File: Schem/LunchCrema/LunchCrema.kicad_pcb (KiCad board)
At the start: 4 copper layers, 160 x 64.4 mm, 52 parts, among them IC1 MMPQ3904, J1 pBITzBus, J3 DE15_Socket_HighDensity_Mount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, SW1 SW_Coded_SH-7070, U1 74HC688, U10 74HC139, U2 V9958, U3 74HC273, U8 74LVC1G19, Y1 HC-49/U-S21477270ABJB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

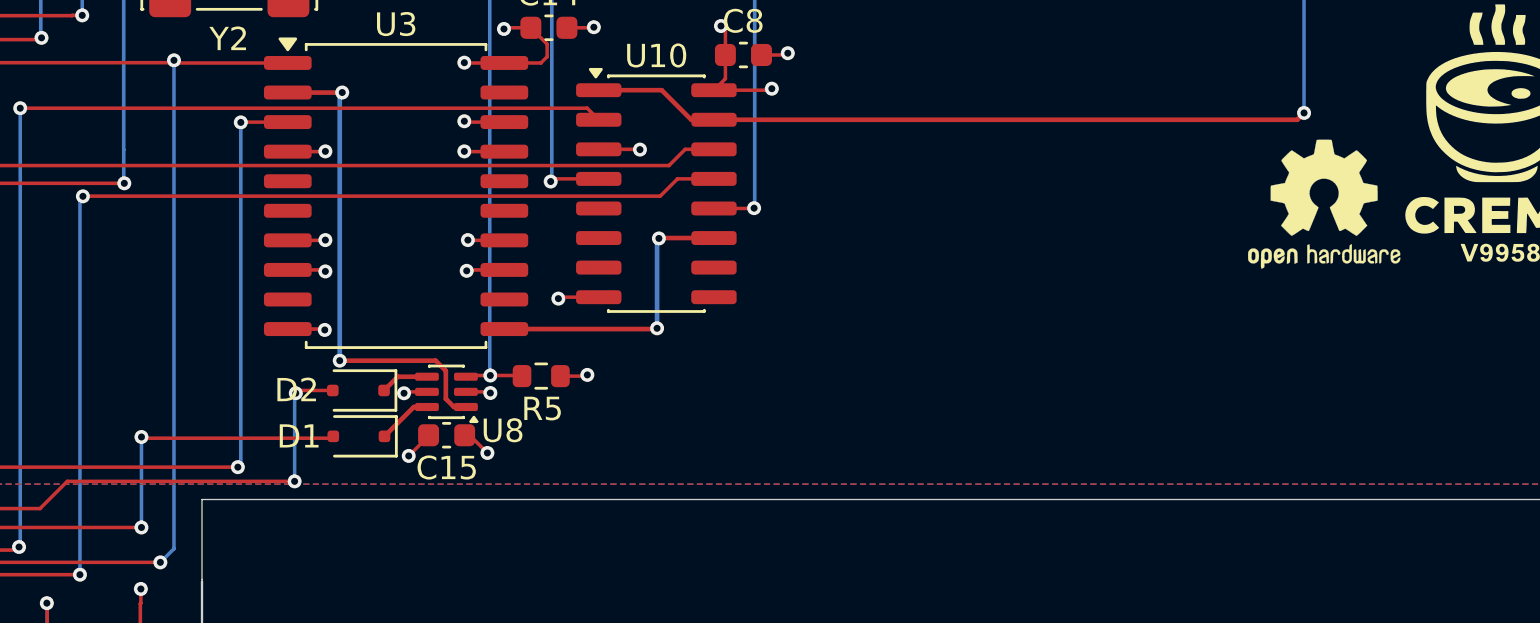
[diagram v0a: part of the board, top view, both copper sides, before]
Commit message: Added both the Morning Joe and the Lunch Crema schematics, PCB, and KiCad library files.
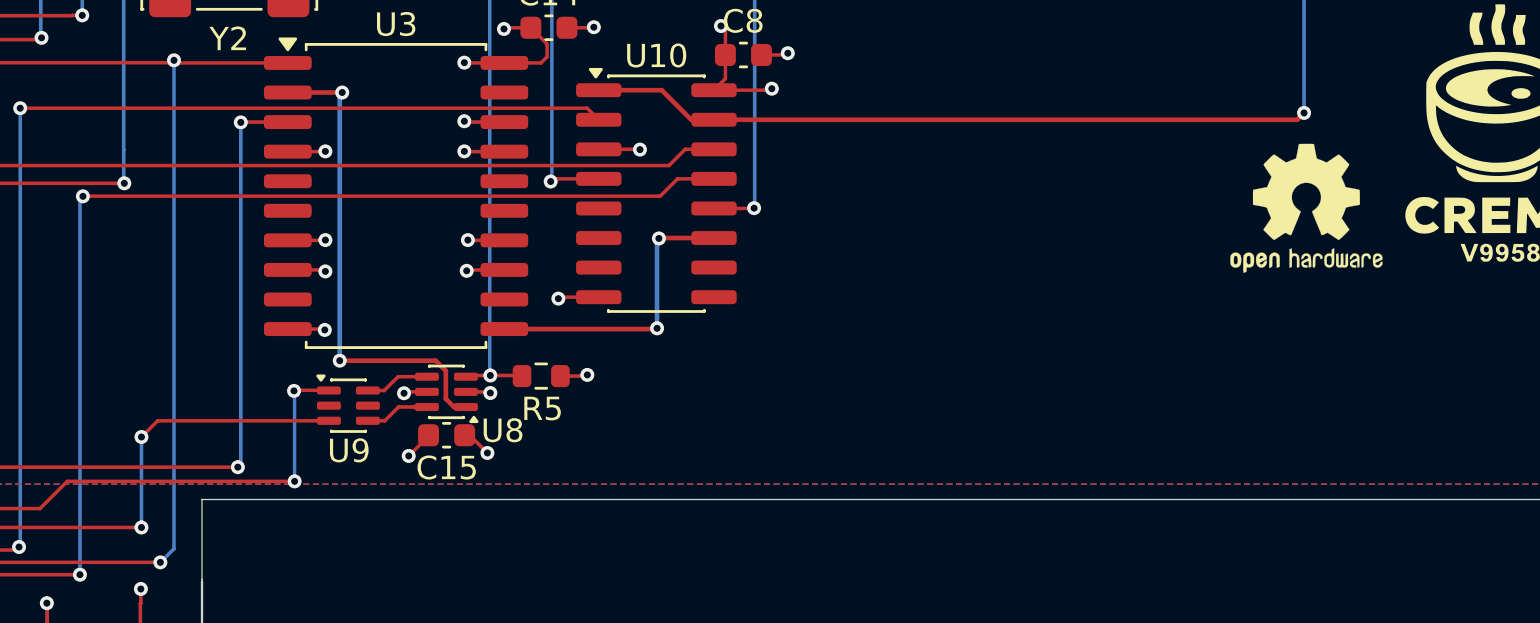
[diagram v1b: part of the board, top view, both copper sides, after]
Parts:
- removed D1, D2: BAT54JW-7-F, Diode_SMD:D_SOD-323F
- added U9: BAT54JW-7-F, Package_TO_SOT_SMD:SOT-363_SC-70-6, F.Cu at (366.7, 168.1)
- moved REF** 0.78 mm to (407.9, 159.6)
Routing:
- net Net-(U8-Y1): track 2.09 -> 2.78 mm

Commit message: Review and Fixes
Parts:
- removed R6: 4k7, Resistor_SMD:R_0603_1608Metric
- removed REF**: OSHW-Logo2_7.3x6mm_SilkScreen, Symbol:OSHW-Logo2_7.3x6mm_SilkScreen
- added R20: 4k7, Resistor_SMD:R_0603_1608Metric, F.Cu at (353.5, 119.9)
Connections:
- U2 pad 27: Net-(U2D-~{HRESET}) -> +5V
- U2 pad 3: unconnected-(U2D-~{DLCLK}-Pad3) -> Net-(U2D-~{DLCLK})
- U2 pad 4: Net-(U2D-~{HRESET}) -> +5V
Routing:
- net Net-(U2D-~{HRESET}): track 45.1 -> 0.00 mm
- net +5V: track 84.2 -> 126.0 mm
- net Net-(U2D-~{DLCLK}): track 0.00 -> 6.42 mm

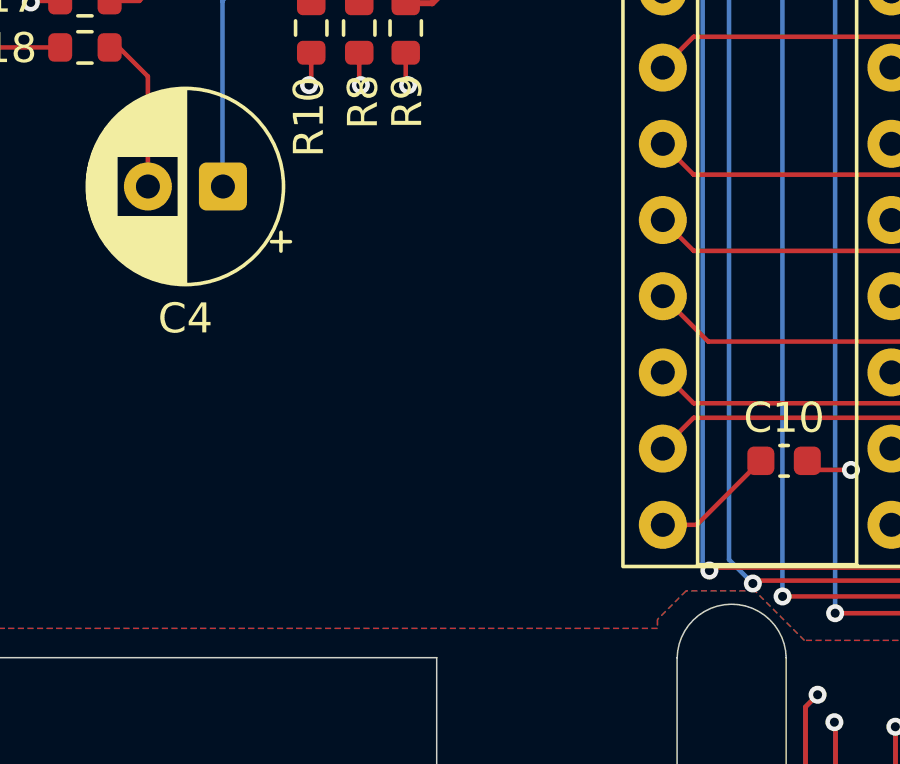
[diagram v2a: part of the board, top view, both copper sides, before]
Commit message: Added bulk caps and fixed up the part numbers
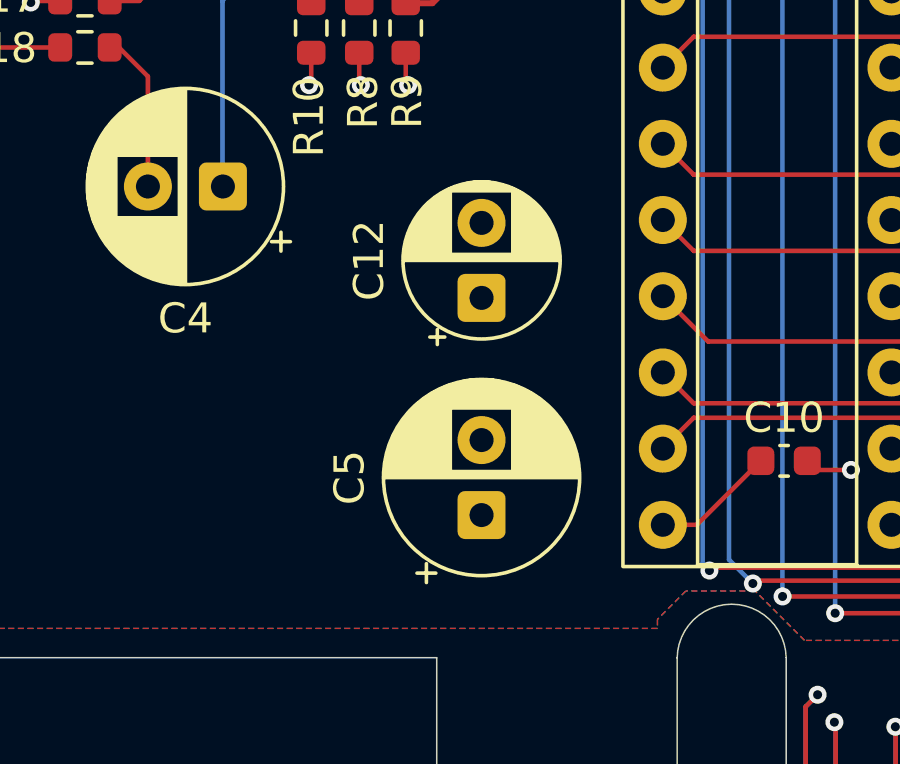
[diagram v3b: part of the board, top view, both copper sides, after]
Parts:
- added C12: 10uF, Capacitor_THT:CP_Radial_D5.0mm_P2.50mm, F.Cu at (299.0, 160.0)
- added C5: 220uF, Capacitor_THT:CP_Radial_D6.3mm_P2.50mm, F.Cu at (299.0, 167.3)

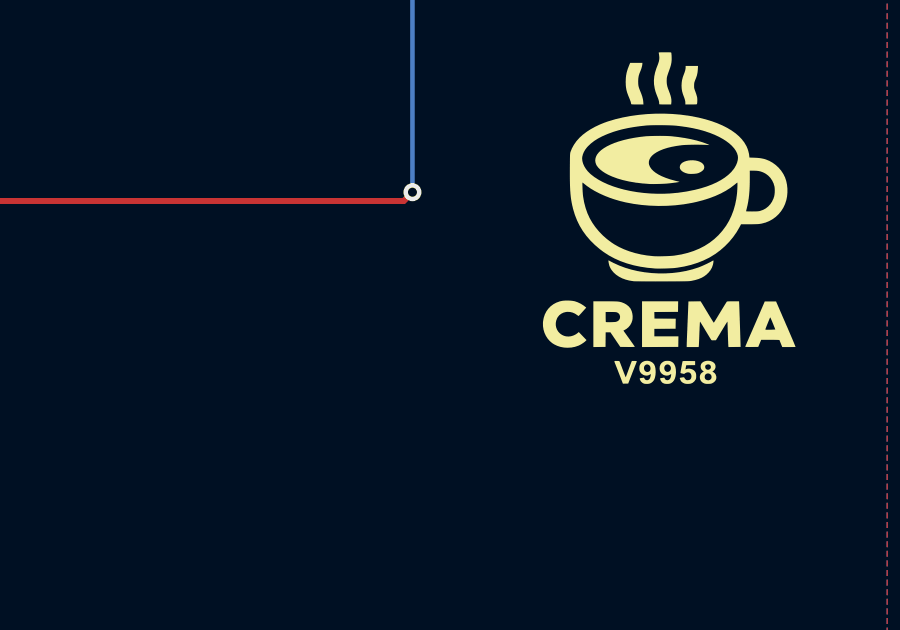
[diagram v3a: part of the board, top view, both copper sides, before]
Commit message: For some reason the OpenSource Hardware Logo had disapeared
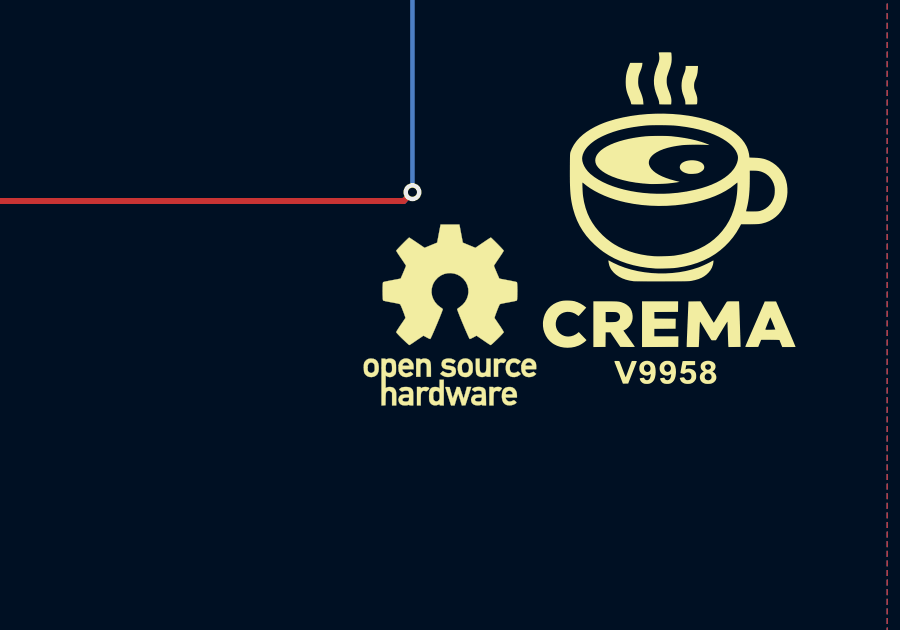
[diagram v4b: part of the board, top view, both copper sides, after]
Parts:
- added REF**: OSHW-Logo_5.7x6mm_SilkScreen, Symbol:OSHW-Logo_5.7x6mm_SilkScreen, F.Cu at (409.0, 159.6)

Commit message: Cosmetic changes
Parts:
- moved J3 3.80 mm to (278.2, 154.2)
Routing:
- net /Video/SYNC: track 28.6 -> 31.5 mm
- net /Video/BLUE: track 7.60 -> 9.17 mm
- net /Video/GREEN: track 6.97 -> 8.17 mm
- net /Video/RED: track 7.31 -> 7.83 mm
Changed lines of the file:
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@@
 	(footprint "Connector_Dsub:DSUB-15-HD_Socket_Horizontal_P2.29x2.54mm_EdgePinOffset8.35mm_Housed_MountingHolesOffset10.89mm"
 		(layer "F.Cu")
-		(at 278.155755 150.3874 -90)
+		(at 278.155755 154.1874 -90)
 		(descr "15-pin D-Sub connector, horizontal/angled (90 deg), THT-mount, socket (female), pitch 2.29x2.54mm, pin-PCB-offset 8.35mm, distance of mounting holes 25mm, distance of mounting holes to PCB edge 10.89mm, see https://disti-assets.s3.amazonaws.com/tonar/files/datasheets/16730.pdf")
 		(tags "15-pin D-Sub connector horizontal angled 90deg THT socket pitch 2.29x2.54mm pin-PCB-offset 8.35mm mounting-holes-distance 25mm mounting-hole-offset 10.89mm")
@@
 		)
 		(point
-			(at 264.725755 146.0724)
+			(at 264.725755 149.8724)
 			(size 2)
 			(layer "F.Fab")
@@
 	)
 	(segment
-		(start 284.9396 151.6644)
-		(end 279.432755 151.6644)
+		(start 280.678755 151.6644)
+		(end 278.155755 154.1874)
 		(width 0.1524)
 		(layer "F.Cu")
@@
 	)
 	(segment
-		(start 279.432755 151.6644)
-		(end 278.155755 150.3874)
+		(start 284.9396 151.6644)
+		(end 280.678755 151.6644)
 		(width 0.1524)
 		(layer "F.Cu")
@@
 	)
 	(segment
-		(start 284.9396 143.8412)
-		(end 280.121955 143.8412)
+		(start 278.155755 149.6074)
+		(end 283.921955 143.8412)
 		(width 0.1524)
 		(layer "F.Cu")
@@
 	)
 	(segment
-		(start 280.121955 143.8412)
-		(end 278.155755 145.8074)
+		(start 283.921955 143.8412)
+		(end 284.9396 143.8412)
 		(width 0.1524)
 		(layer "F.Cu")
@@
 	)
 	(segment
-		(start 282.1306 142.256)
-		(end 277.186816 142.256)
+		(start 284.9174 139.4248)
+		(end 284.9396 139.447)
 		(width 0.1524)
 		(layer "F.Cu")
@@
 	)
 	(segment
-		(start 284.9174 139.4248)
-		(end 284.9396 139.447)
+		(start 278.077494 142.256)
+		(end 274.104355 146.229139)
 		(width 0.1524)
 		(layer "F.Cu")
@@
 	)
 	(segment
-		(start 273.075755 145.747739)
-		(end 273.075755 145.8074)
+		(start 274.104355 146.229139)
+		(end 274.104355 148.5788)
 		(width 0.1524)
 		(layer "F.Cu")
@@
 	)
 	(segment
-		(start 277.186816 142.256)
-		(end 275.809016 143.6338)
+		(start 297.8116 138.7394)
+		(end 285.6472 138.7394)
 		(width 0.1524)
 		(layer "F.Cu")
@@
 	)
 	(segment
-		(start 275.809016 143.6338)
-		(end 275.189694 143.6338)
+		(start 285.6472 138.7394)
+		(end 284.9396 139.447)
 		(width 0.1524)
 		(layer "F.Cu")
@@
 	)
 	(segment
-		(start 297.8116 138.7394)
-		(end 285.6472 138.7394)
+		(start 274.104355 148.5788)
+		(end 273.075755 149.6074)
 		(width 0.1524)
 		(layer "F.Cu")
@@
 	)
 	(segment
-		(start 285.6472 138.7394)
-		(end 284.9396 139.447)
+		(start 282.1306 142.256)
+		(end 278.077494 142.256)
 		(width 0.1524)
 		(layer "F.Cu")
@@
 	)
 	(segment
-		(start 275.189694 143.6338)
-		(end 273.075755 145.747739)
+		(start 281.512955 148.5402)
+		(end 278.155755 151.8974)
 		(width 0.1524)
 		(layer "F.Cu")
-		(net "/Video/SYNC")
+		(net "/Video/GREEN")
 	)
 	(segment
-		(start 278.598555 148.5402)
-		(end 278.155755 148.0974)
+		(start 284.9396 148.5402)
+		(end 281.512955 148.5402)
 		(width 0.1524)
 		(layer "F.Cu")
@@
 	)
 	(segment
-		(start 284.9396 148.5402)
-		(end 278.598555 148.5402)
+		(start 273.075755 145.747739)
+		(end 273.075755 145.8074)
 		(width 0.1524)
 		(layer "F.Cu")
-		(net "/Video/GREEN")
+		(net "unconnected-(J3-Pad15)")
 	)
 	(segment

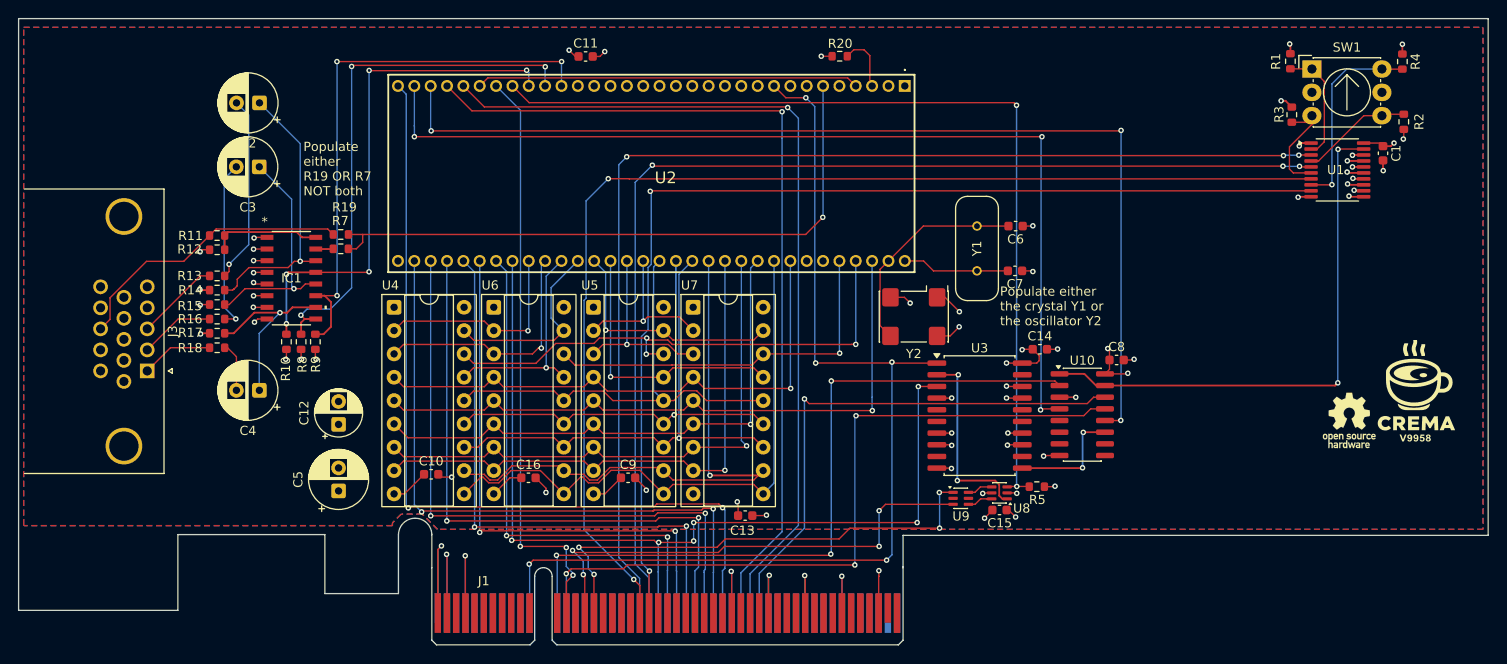
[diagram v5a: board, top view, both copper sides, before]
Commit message: Nasty fix for the Lunch Crema..... the pBITz interface bus connector was mirrored!
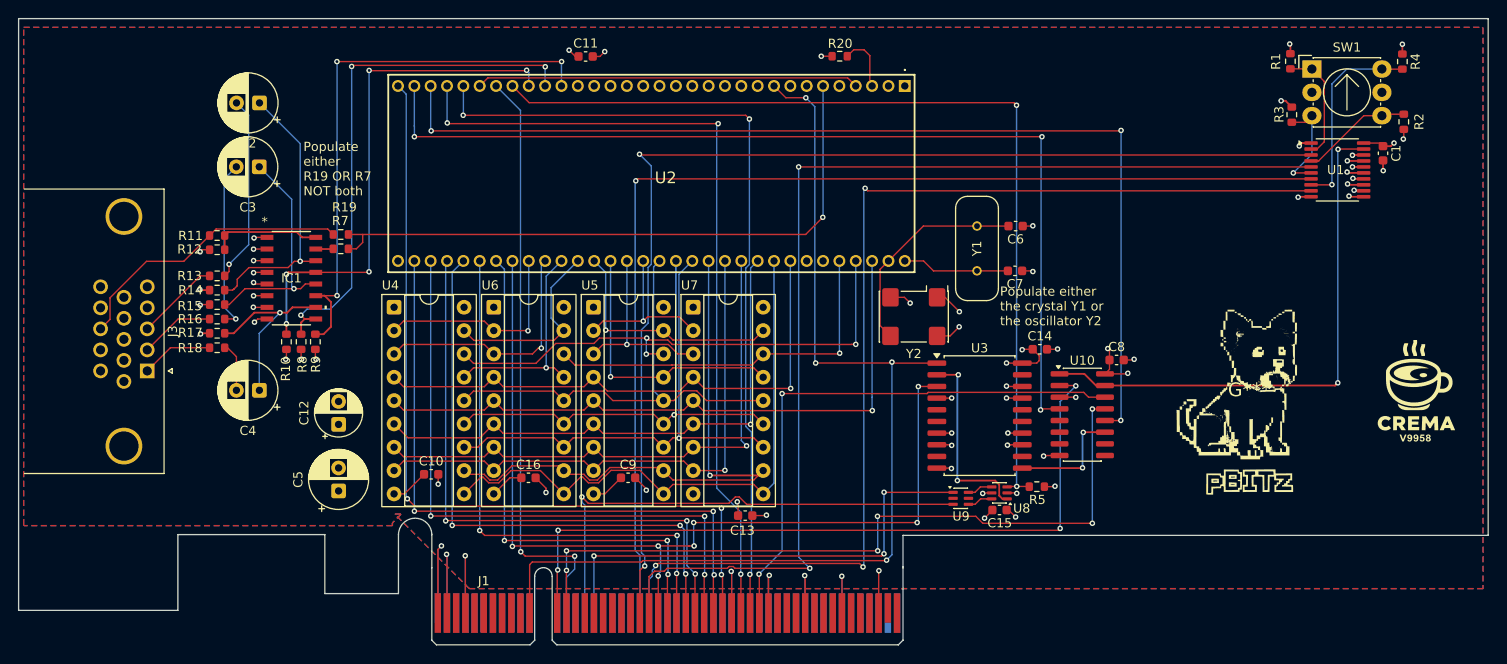
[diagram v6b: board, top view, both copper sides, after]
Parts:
- removed REF**: OSHW-Logo_5.7x6mm_SilkScreen, Symbol:OSHW-Logo_5.7x6mm_SilkScreen
- added G***: LOGO, Footprints:pBITzlogo-Silk, F.Cu at (398.1, 156.2)
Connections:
- J1 pad A11: /Video/~{RESET} -> unconnected-(J1A-CTRL_10-PadA11)
- J1 pad A12: /Video/~{RD} -> unconnected-(J1A-CTRL_11-PadA12)
- J1 pad A13: /Video/~{WR} -> /Video/~{WAIT}
- J1 pad A15: unconnected-(J1A-CTRL_14-PadA15) -> /Video/~{INT}
- J1 pad A16: unconnected-(J1A-CTRL_15-PadA16) -> /Video/~{NMI}
- J1 pad A21: /Device Select Decode/CS0 -> /Device Select Decode/CS2
- J1 pad A22: /Device Select Decode/CS1 -> /Device Select Decode/CS3
- J1 pad A23: /Video/D0 -> unconnected-(J1A-D8-PadA23)
- J1 pad A24: /Video/D1 -> unconnected-(J1A-D9-PadA24)
- J1 pad A25: /Video/D2 -> unconnected-(J1A-D10-PadA25)
- J1 pad A26: /Video/D3 -> unconnected-(J1A-D11-PadA26)
- J1 pad A27: /Video/D4 -> unconnected-(J1A-D12-PadA27)
- J1 pad A28: /Video/D5 -> unconnected-(J1A-D13-PadA28)
- J1 pad A29: /Video/D6 -> unconnected-(J1A-D14-PadA29)
- J1 pad A30: /Video/D7 -> unconnected-(J1A-D15-PadA30)
- J1 pad A32: /Video/A0 -> unconnected-(J1A-A12-PadA32)
- J1 pad A33: /Video/A1 -> unconnected-(J1A-A13-PadA33)
- J1 pad A34: /Video/A2 -> unconnected-(J1A-A14-PadA34)
- J1 pad B11: unconnected-(J1A-CTRL_0-PadB11) -> /Video/~{RESET}
- J1 pad B12: unconnected-(J1A-CTRL_1-PadB12) -> /Video/~{RD}
- J1 pad B13: /Video/~{WAIT} -> /Video/~{WR}
- J1 pad B15: /Video/~{INT} -> unconnected-(J1A-CTRL_4-PadB15)
- J1 pad B16: /Video/~{NMI} -> unconnected-(J1A-CTRL_5-PadB16)
- J1 pad B21: /Device Select Decode/CS2 -> /Device Select Decode/CS0
- J1 pad B22: /Device Select Decode/CS3 -> /Device Select Decode/CS1
- J1 pad B23: unconnected-(J1A-D0-PadB23) -> /Video/D0
- J1 pad B24: unconnected-(J1A-D1-PadB24) -> /Video/D1
- J1 pad B25: unconnected-(J1A-D2-PadB25) -> /Video/D2
- J1 pad B26: unconnected-(J1A-D3-PadB26) -> /Video/D3
- J1 pad B27: unconnected-(J1A-D4-PadB27) -> /Video/D4
- J1 pad B28: unconnected-(J1A-D5-PadB28) -> /Video/D5
- J1 pad B29: unconnected-(J1A-D6-PadB29) -> /Video/D6
- J1 pad B30: unconnected-(J1A-D7-PadB30) -> /Video/D7
- J1 pad B32: unconnected-(J1A-A0-PadB32) -> /Video/A0
- J1 pad B33: unconnected-(J1A-A1-PadB33) -> /Video/A1
- J1 pad B34: unconnected-(J1A-A2-PadB34) -> /Video/A2
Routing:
- net /Device Select Decode/CS2: track 127.4 -> 120.9 mm, vias 2 -> 1
- net /Video/A0: track 94.1 -> 88.0 mm, vias 1 -> 3
- net /Video/A1: track 94.0 -> 88.8 mm, vias 1 -> 3
- net /Video/~{WR}: track 79.8 -> 82.0 mm, vias 3 -> 6
- net /Video/D3: track 62.1 -> 63.9 mm, vias 2 -> 3
- net /Video/A2: track 58.6 -> 60.4 mm, vias 1 -> 2
- net /Video/~{RD}: track 80.2 -> 81.8 mm, vias 3 -> 4
- net /Video/~{NMI}: track 53.6 -> 52.1 mm, vias 4 -> 3
- net /Video/D4: track 66.4 -> 65.1 mm, vias 2 -> 3
- net /Video/D7: track 92.7 -> 91.5 mm, vias 2 -> 3
- net /Device Select Decode/CS0: track 125.6 -> 124.5 mm, vias 3 -> 2
- net /Video/D0: track 101.4 -> 102.2 mm, vias 6 -> 7
- net GND: track 108.7 -> 108.0 mm
- net /Video/~{INT}: track 53.4 -> 54.1 mm, vias 4 -> 1
- net /Video/D5: track 68.7 -> 68.2 mm, vias 2 -> 3
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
